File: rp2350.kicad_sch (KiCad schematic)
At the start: 39 parts, among them J1 SM03B-SRSS-TB, SW2 SW_Push, SW3 SW_Push, U6 W25Q32JVZPIQ, U7 NCP1117-3.3_SOT223, U8 RP2350_60QFN, Y1 ABM8-272-T3

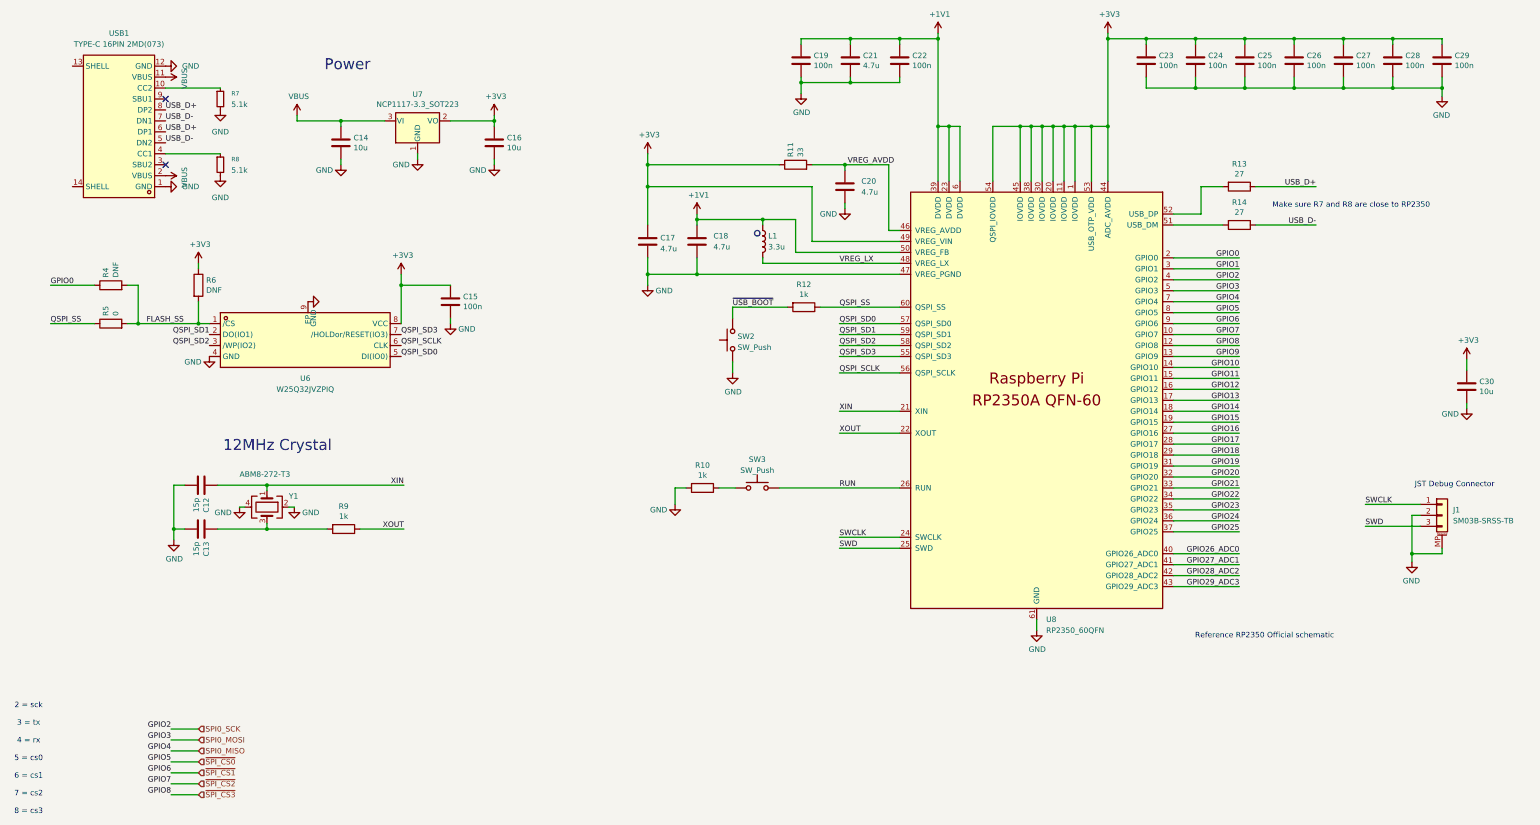
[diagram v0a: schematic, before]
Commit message: complete component alignment
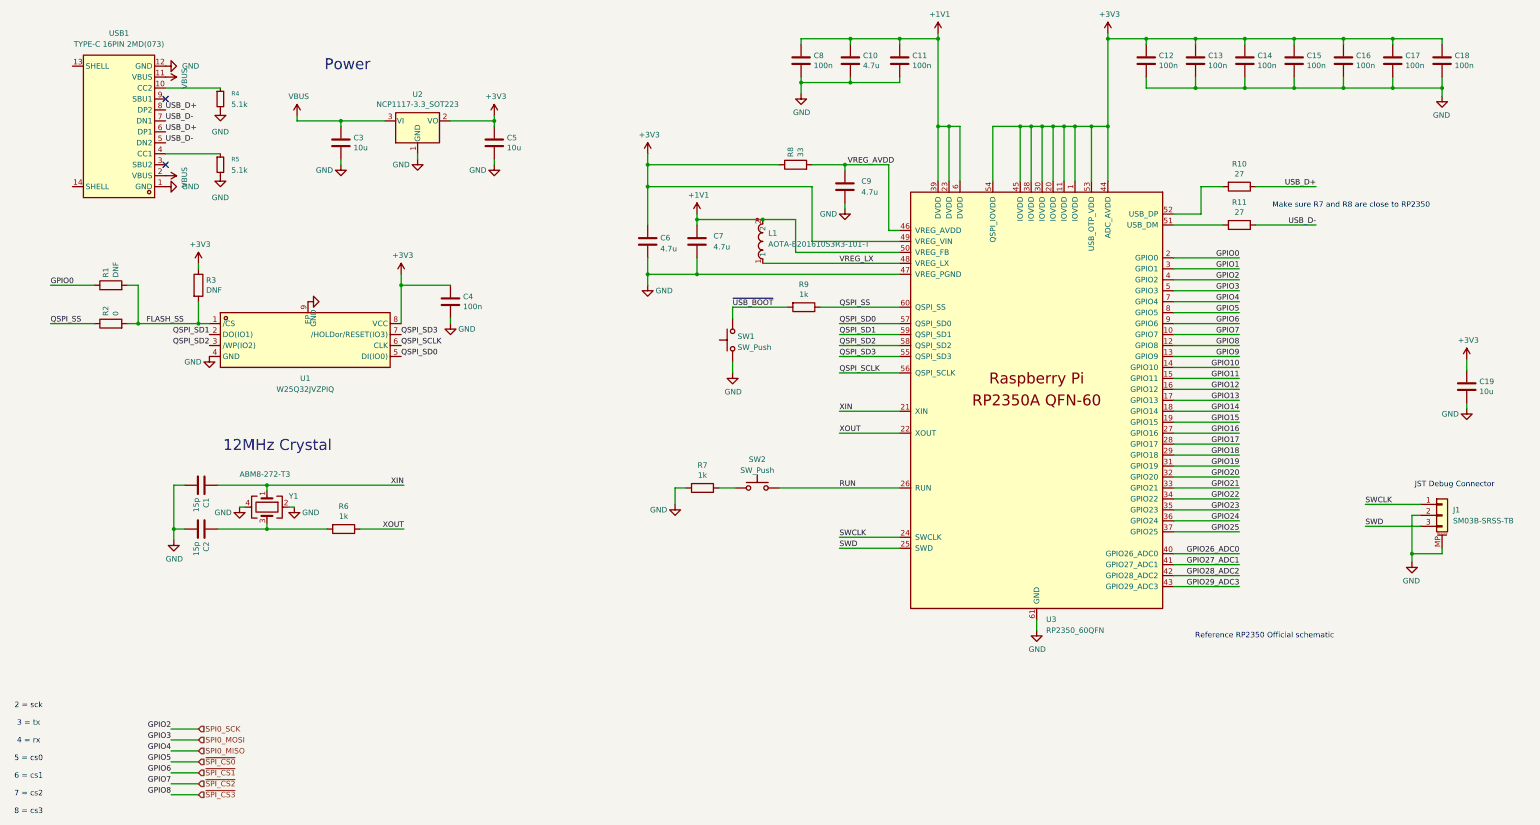
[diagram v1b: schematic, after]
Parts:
- removed L1: 3.3u, RP2350_60QFN_minimal:L_pol_2016, symbol Device:L
- added L1: AOTA-B201610S3R3-101-T, rtd-transmitter-library:IND-SMD_L2.0-W1.6_AOTA-B201610S3R3-101-T, symbol rtd-transmitter-library:AOTA-B201610S3R3-101-T
- C1: renamed from C12; footprint Capacitor_SMD:C_0402_1005Metric -> Capacitor_SMD:C_0603_1608Metric
- C10: renamed from C21; footprint Capacitor_SMD:C_0402_1005Metric -> Capacitor_SMD:C_0603_1608Metric
- C11: renamed from C22; footprint Capacitor_SMD:C_0402_1005Metric -> Capacitor_SMD:C_0603_1608Metric
- C12: renamed from C23; footprint Capacitor_SMD:C_0402_1005Metric -> Capacitor_SMD:C_0603_1608Metric
- C13: renamed from C24; footprint Capacitor_SMD:C_0402_1005Metric -> Capacitor_SMD:C_0603_1608Metric
- C14: renamed from C25; footprint Capacitor_SMD:C_0402_1005Metric -> Capacitor_SMD:C_0603_1608Metric
- C15: renamed from C26; footprint Capacitor_SMD:C_0402_1005Metric -> Capacitor_SMD:C_0603_1608Metric
- C16: renamed from C27; footprint Capacitor_SMD:C_0402_1005Metric -> Capacitor_SMD:C_0603_1608Metric
- C17: renamed from C28; footprint Capacitor_SMD:C_0402_1005Metric -> Capacitor_SMD:C_0603_1608Metric
- C18: renamed from C29; footprint Capacitor_SMD:C_0402_1005Metric -> Capacitor_SMD:C_0603_1608Metric
- C19: renamed from C30; footprint Capacitor_SMD:C_0805_2012Metric -> Capacitor_SMD:C_0603_1608Metric
- C2: renamed from C13; footprint Capacitor_SMD:C_0402_1005Metric -> Capacitor_SMD:C_0603_1608Metric
- C3: renamed from C14; footprint Capacitor_SMD:C_0805_2012Metric -> Capacitor_SMD:C_0603_1608Metric
- C4: renamed from C15; footprint Capacitor_SMD:C_0402_1005Metric -> Capacitor_SMD:C_0603_1608Metric
- C5: renamed from C16; footprint Capacitor_SMD:C_0805_2012Metric -> Capacitor_SMD:C_0603_1608Metric
- C6: renamed from C17; footprint RP2350_60QFN_minimal:C_0402_1005Metric_small_pads -> Capacitor_SMD:C_0603_1608Metric
- C7: renamed from C18; footprint RP2350_60QFN_minimal:C_0402_1005Metric_small_pads -> Capacitor_SMD:C_0603_1608Metric
- C8: renamed from C19; footprint Capacitor_SMD:C_0402_1005Metric -> Capacitor_SMD:C_0603_1608Metric
- C9: renamed from C20; footprint Capacitor_SMD:C_0402_1005Metric -> Capacitor_SMD:C_0603_1608Metric
- R1: renamed from R4; footprint Resistor_SMD:R_0402_1005Metric -> Resistor_SMD:R_0603_1608Metric
- R10: renamed from R13; footprint Resistor_SMD:R_0402_1005Metric -> Resistor_SMD:R_0603_1608Metric
- R11: renamed from R14; footprint Resistor_SMD:R_0402_1005Metric -> Resistor_SMD:R_0603_1608Metric
- R2: renamed from R5; footprint Resistor_SMD:R_0402_1005Metric -> Resistor_SMD:R_0603_1608Metric
- R3: renamed from R6; footprint Resistor_SMD:R_0402_1005Metric -> Resistor_SMD:R_0603_1608Metric
- R4: renamed from R7; footprint (none) -> Resistor_SMD:R_0603_1608Metric
- R5: renamed from R8; footprint (none) -> Resistor_SMD:R_0603_1608Metric
- R6: renamed from R9; footprint Resistor_SMD:R_0402_1005Metric -> Resistor_SMD:R_0603_1608Metric
- R7: renamed from R10; footprint Resistor_SMD:R_0402_1005Metric -> Resistor_SMD:R_0603_1608Metric
- R8: renamed from R11; footprint Resistor_SMD:R_0402_1005Metric -> Resistor_SMD:R_0603_1608Metric
- R9: renamed from R12; footprint Resistor_SMD:R_0402_1005Metric -> Resistor_SMD:R_0603_1608Metric
- U3: renamed from U8; footprint RP2350_60QFN_minimal:RP2350-QFN-60-1EP_7x7_P0.4mm_EP3.4x3.4mm_ThermalVias -> Package_DFN_QFN:QFN-60-1EP_7x7mm_P0.4mm_EP3.4x3.4mm_ThermalVias
- renumbered SW2 to SW1, SW3 to SW2, U6 to U1, U7 to U2
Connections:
- net +1V1: now also L1.2
- net VREG_LX: now also L1.1

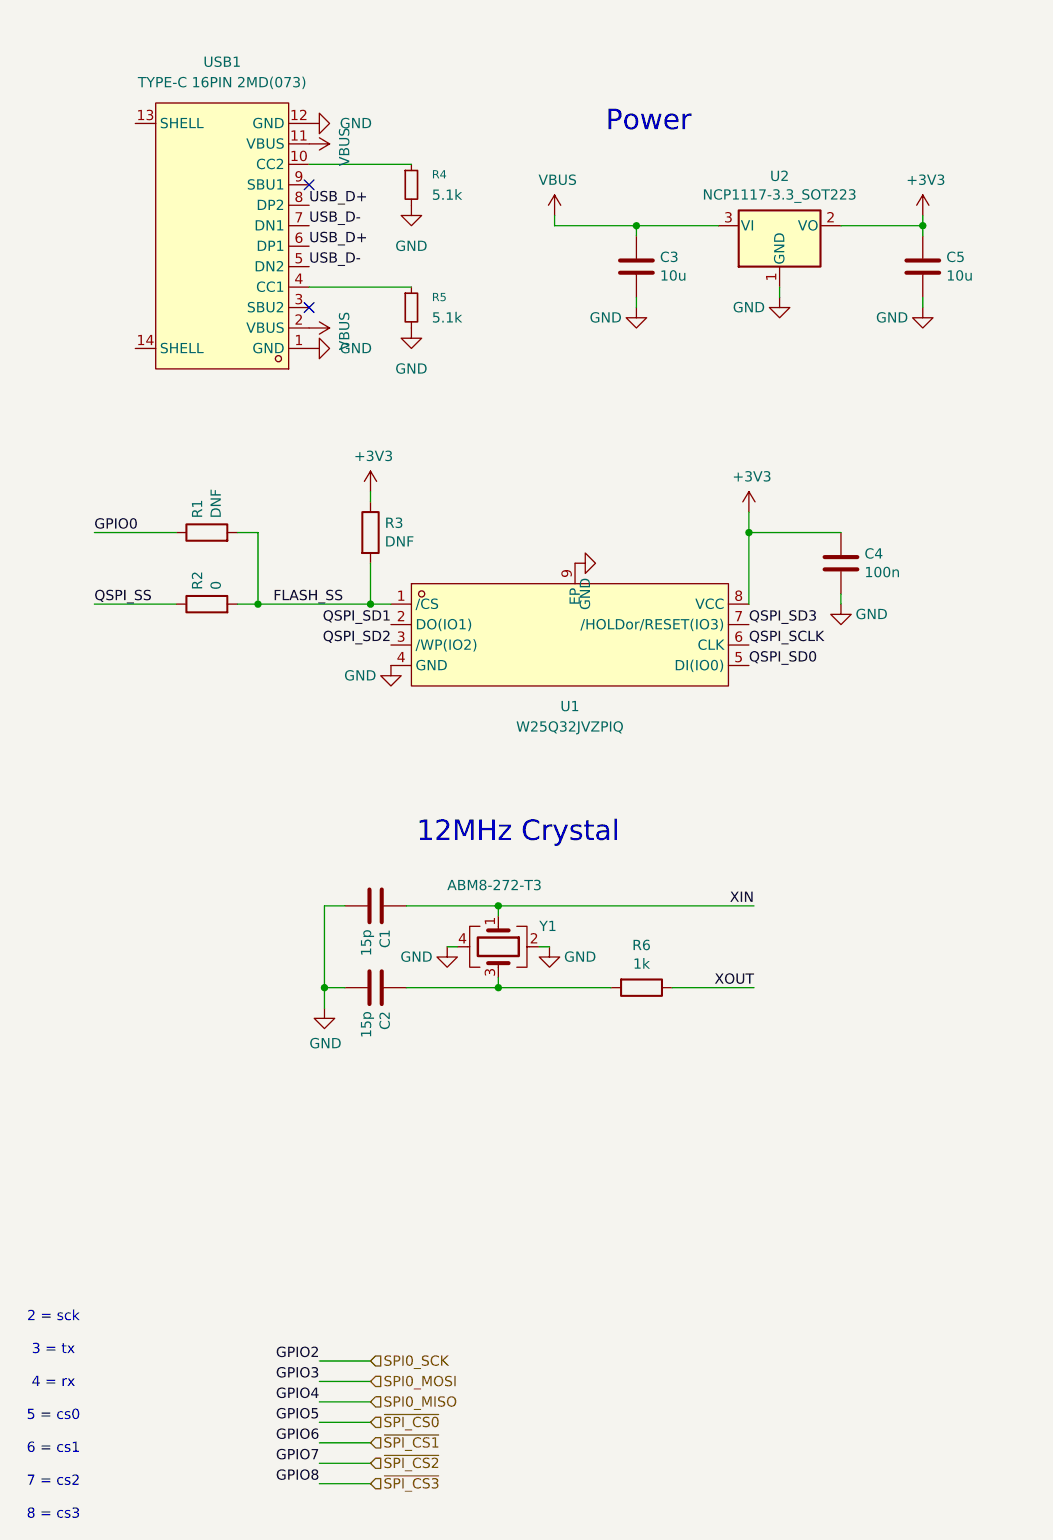
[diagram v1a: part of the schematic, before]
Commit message: start pcb layout, add sd card and screen
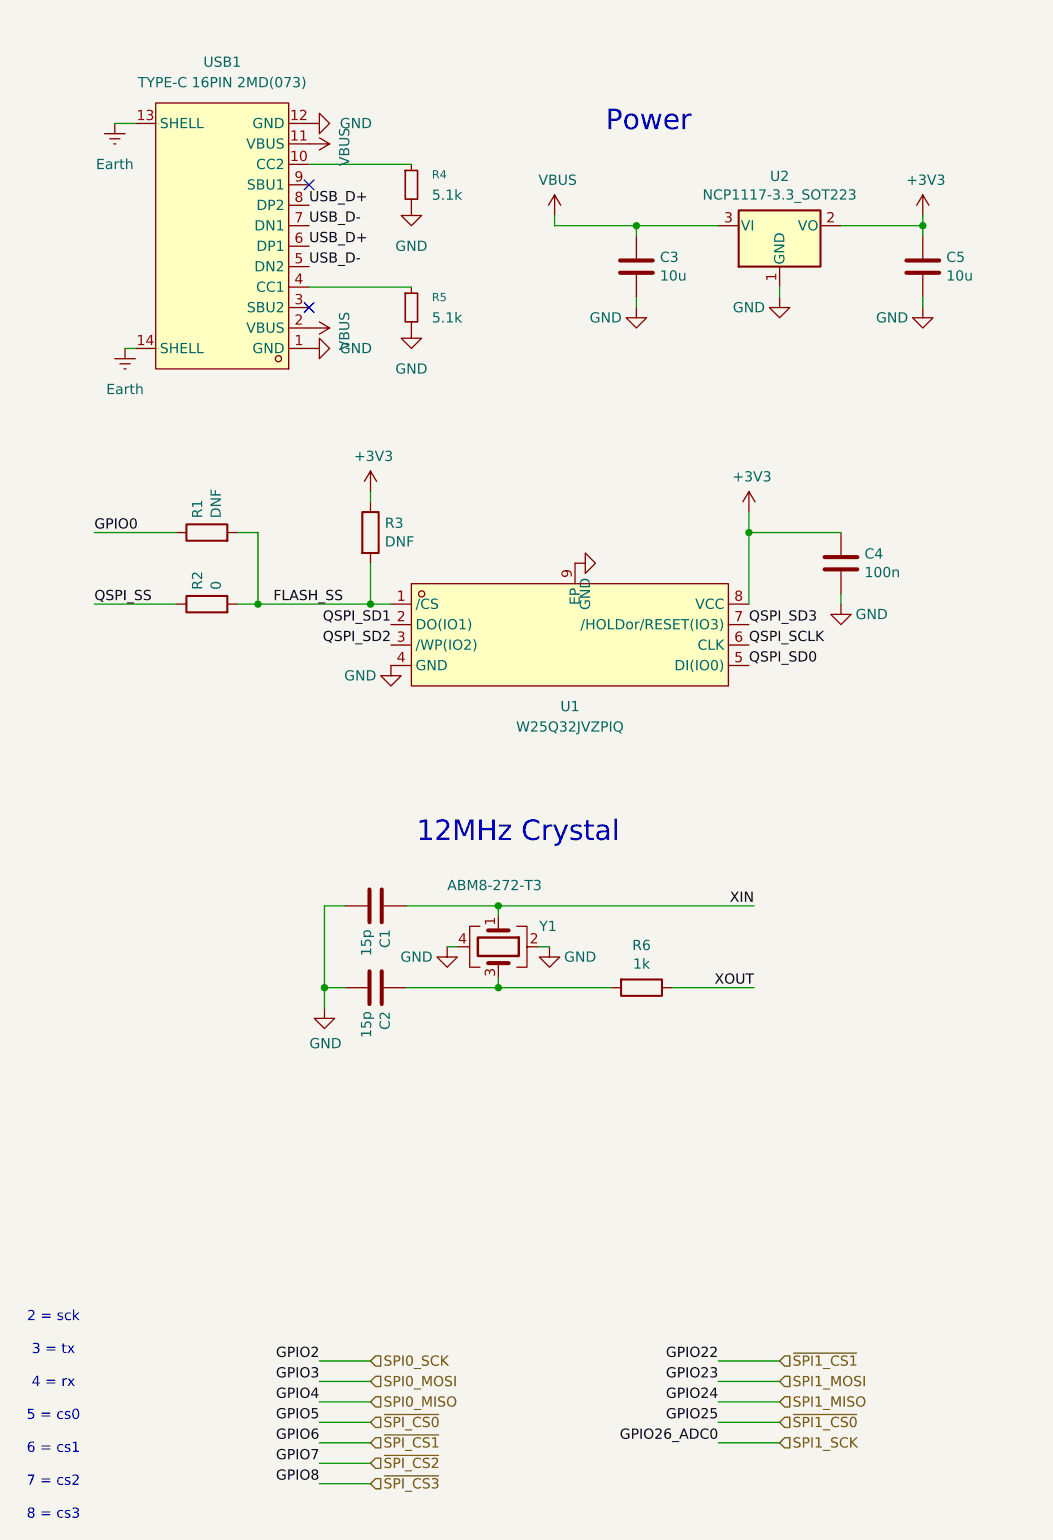
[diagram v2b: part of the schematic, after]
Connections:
- net Earth: now reaches USB1.13 (SHELL)
- net Earth: now also USB1.14 (SHELL)
- net GPIO22 renamed ~{SPI1_CS1}
- net GPIO23 renamed SPI1_MOSI
- net GPIO24 renamed SPI1_MISO
- net GPIO25 renamed ~{SPI1_CS0}
- net GPIO26_ADC0 renamed SPI1_SCK

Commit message: Complete single channel design
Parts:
- added SW7: OS4D501110, rtd-transmitter-library:SW-SMD_L6.0-W6.0-P6.00-LS6.8, symbol rtd-transmitter-library:OS4D501110
